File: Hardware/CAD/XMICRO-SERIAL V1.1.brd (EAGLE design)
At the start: 203.2 x 101.6 mm, 92 parts, among them J1 D9-MPH, J2 D9-MPH, J3 MINI-DIN6, J4 PINHD1X3, J5 PINHD1X3, Q1 2N5088, Q2 2N5088, Q3 2N5088, U1 555, U10 74280, U11 74273, U12 74164, U13 74164, U14 7474, U15 74244, U16 74244, U17 74240, U18 74280, U19 74165, U2 7486, U20 74165, U21 74244, U22 7404, U23 74245, U24 16550, U25 16550, U26 75185, U27 75185, U3 7410, U4 7404, U5 7474, U6 7474, U7 7408, U8 74138, U9 74138, Y1 1.8432MHz

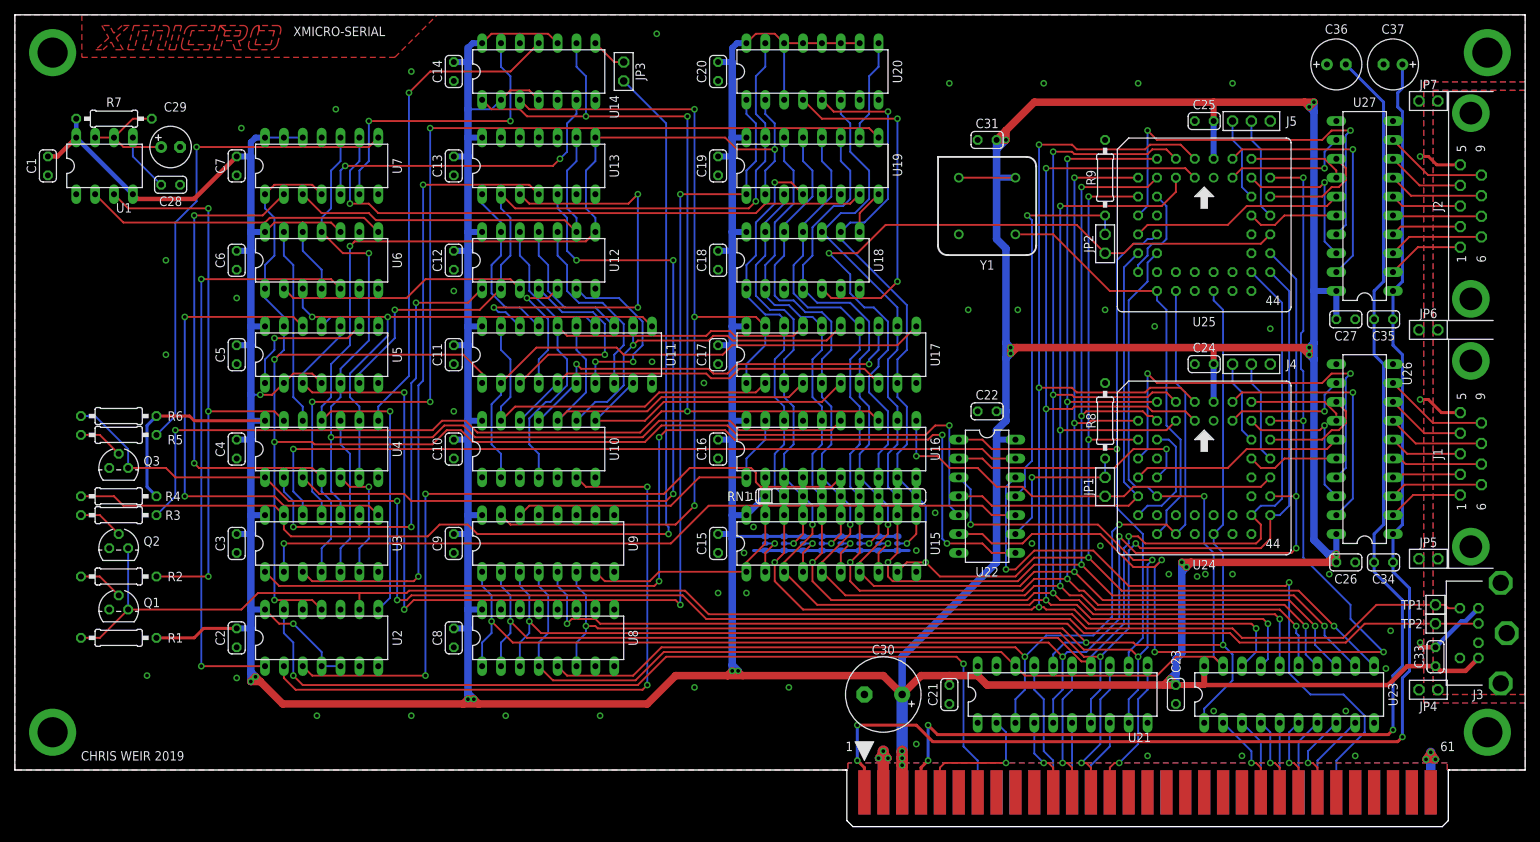
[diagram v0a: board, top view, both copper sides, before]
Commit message: Updated design to V1.1 - added Schmitt trigger inputs, improved connector spacing, fixed PS/2 connector footprint
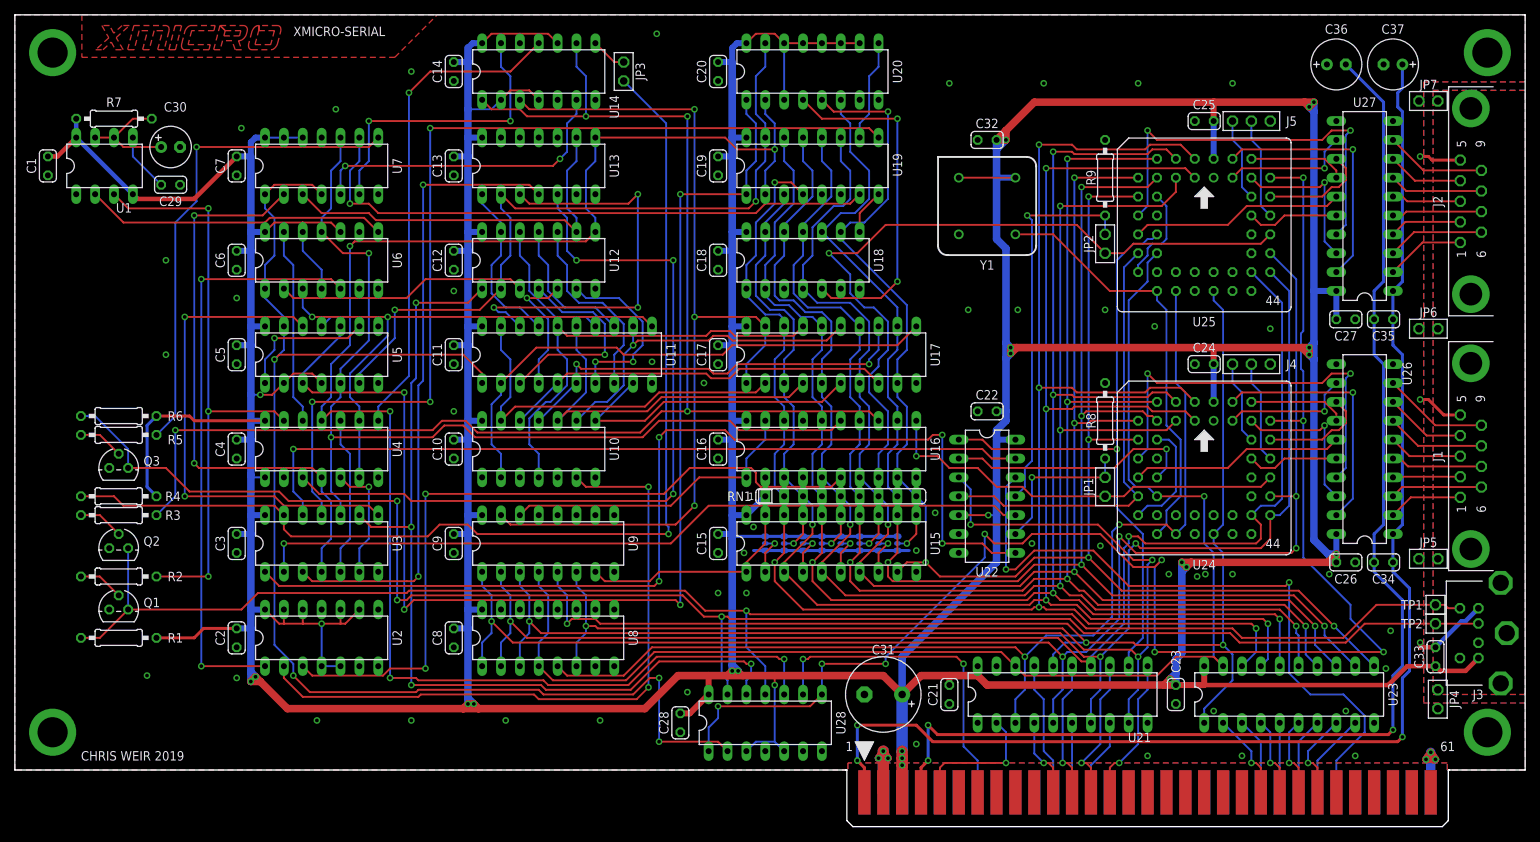
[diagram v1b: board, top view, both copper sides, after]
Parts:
- added C32: 0.1uF, Custom:C100
- added U28: 7414, 74xx-us:DIL14
- C28: value 10nF -> 0.1uF
- C29: value 0.1uF -> 10nF; device rcl:E2,5-6 -> Custom:C100
- C30: value 220uF -> 0.1uF; device Custom:C-10-5 -> rcl:E2,5-6
- C31: value 0.1uF -> 220uF; device Custom:C100 -> Custom:C-10-5
- moved C30 120.9 mm to (21.0, 83.8), turned to 0 degrees
- moved C28 99.7 mm to (89.5, 6.35), turned to 270 degrees
- moved C31 75.9 mm to (116.8, 10.2)
- moved C29 5.08 mm to (21.0, 78.7)
- moved JP4 1.80 mm to (191.5, 9.53), turned to 90 degrees
- moved J2 0.64 mm to (195.9, 76.5)
- moved J1 0.32 mm to (195.9, 42.2)
- moved JP6 0.16 mm to (190.2, 59.4)
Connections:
- removed net N$26: U22.6, U24.39, U25.39
- new net RST: U24.39, U25.39, U28.1, U28.8
- net !BRST: now also U28.9; no longer U2.13
- net !KB_DATA: now also U28.12; no longer U4.2
- net !RST: now also U28.2; no longer U2.11, U22.5
- net BUFF_KB_CLOCK: now also U28.10; no longer U2.8
- net GND: now also C29.P$2, C31.-, C32.P$2, U28.7; no longer C29.-, C31.P$2, U2.10, U2.12
- net KB_CLOCK: now also U28.11; no longer U2.9
- net KB_DATA: now also U28.13; no longer U4.1
- net N$133: now also C30.+; no longer C29.+
- net N$140: now also C29.P$1; no longer C28.P$1
- net VCC: now also C28.P$1, C31.+, C32.P$1, U2.10, U2.12, U2.13, U2.9, U22.5, U28.14, U28.3, U28.5, U4.1; no longer C30.+, C31.P$1
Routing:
- net RST: track 0.00 -> 205.0 mm, vias 0 -> 9
- net N$26: track 151.6 -> 0.00 mm, vias 5 -> 0
- net !BRST: track 120.2 -> 45.0 mm
- net BUFF_KB_CLOCK: track 152.6 -> 221.0 mm, vias 3 -> 5
- net !KB_DATA: track 64.8 -> 121.1 mm, vias 3 -> 4
- net VCC: track 1061.6 -> 1106.1 mm, vias 22 -> 24
- net !RST: track 210.3 -> 177.4 mm
- net KB_DATA: track 211.5 -> 222.3 mm, vias 2 -> 3
- net KB_CLOCK: track 203.3 -> 213.4 mm, vias 0 -> 1
- net N$101: track 88.1 -> 89.9 mm
- net KB_ERR: track 101.1 -> 100.6 mm
- net GND: track 80.5 -> 80.3 mm, vias 62 -> 61
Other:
- board text added: "V1.1 1943"
- board text removed: "V1.1 1912"

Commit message: Fixed a schematic issue - added second inverter to BUFF_KB_CLOCK signal.
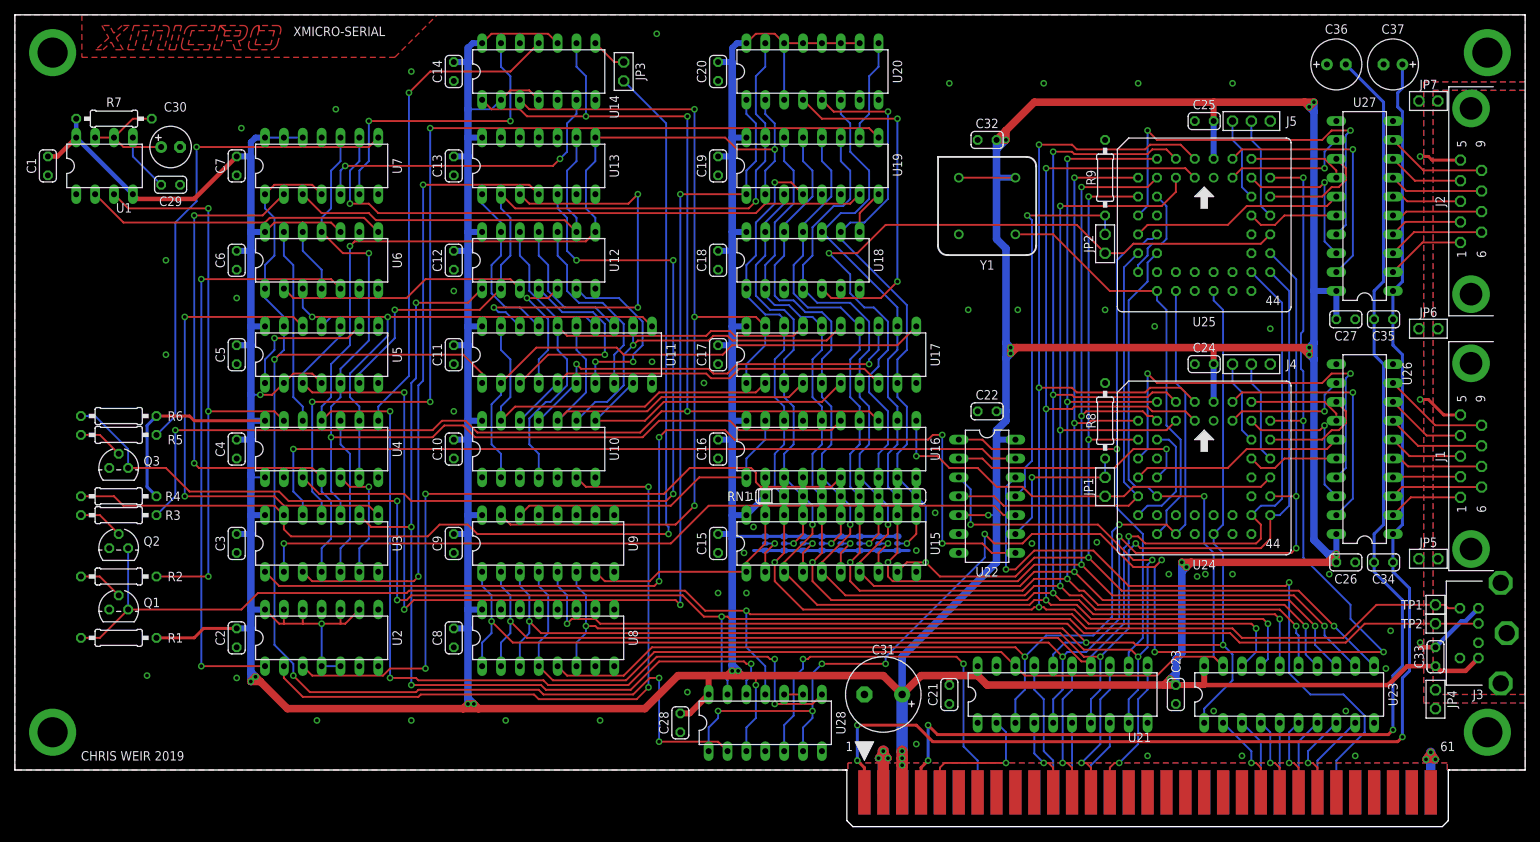
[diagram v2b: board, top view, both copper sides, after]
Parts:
- moved J1 9.53 mm to (205.4, 42.2)
- moved J2 9.53 mm to (205.4, 76.5)
- moved J3 6.35 mm to (205.4, 18.4)
- moved JP4 0.32 mm to (191.1, 9.53)
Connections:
- new net N$26: U28.10, U28.9
- net !BRST: now also U28.5; no longer U28.9
- net BUFF_KB_CLOCK: now also U28.8; no longer U28.10
- net RST: now also U28.6; no longer U28.8
- net VCC: no longer U28.5
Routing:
- net !BRST: track 45.0 -> 53.6 mm
- net BUFF_KB_CLOCK: track 221.0 -> 227.9 mm, vias 5 -> 6
- net RST: track 205.0 -> 211.1 mm, vias 9 -> 10
- net VCC: track 1106.1 -> 1101.8 mm
- net N$26: track 0.00 -> 2.54 mm
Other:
- board text added: "J1 INT"
- board text added: "J2 INT"
- board text added: "KB INT"

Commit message: Updated to hardware V1.1.
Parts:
- removed C35: 0.1uF, Custom:C100
- removed C36, C37: 100uF, rcl:E2,5-7
- added C38, C39: 10uF, rcl:E2,5-5
- added C40: 0.1uF, Custom:C100
- added U29: TC962, Custom:DIL8
- C34: value 0.1uF -> 10uF; device Custom:C100 -> rcl:E2,5-5
- RN1: device resistor-sil:SIL9 -> Custom:SIL9
- moved C34 62.6 mm to (125.4, 49.5), turned to 90 degrees
- moved C32 7.94 mm to (130.8, 92.7)
- moved Y1 7.94 mm to (130.8, 83.8)
- moved C26 2.54 mm to (181.6, 27.9)
- moved C27 2.54 mm to (181.6, 60.6)
- moved JP3 2.54 mm to (84.5, 94.0)
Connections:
- new net N$27: C38.-, U29.4
- new net N$43: C38.+, U29.2
- net +12V: now also C34.+, C40.P$1, U29.8; no longer C34.P$1, C35.P$1, C37.+
- net -12V: now also C39.-, U29.5; no longer C34.P$2, C35.P$2, C36.-, CE0.7
- net GND: now also C34.-, C39.+, C40.P$2, U29.3; no longer C36.+, C37.-
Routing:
- net -12V: track 170.6 -> 96.5 mm, vias 3 -> 1
- net N$116: track 57.5 -> 67.7 mm, vias 0 -> 2
- net N$27: track 0.00 -> 7.83 mm, vias 0 -> 1
- net VCC: track 1101.8 -> 1109.1 mm
- net N$43: track 0.00 -> 5.29 mm
- net A4: track 146.4 -> 149.1 mm
- net N$25: track 137.7 -> 140.2 mm
- net !INT_KB: track 4.86 -> 7.40 mm
- net INT_UART2: track 100.4 -> 98.6 mm
- net N$118: track 52.0 -> 50.7 mm
- net N$24: track 147.1 -> 146.0 mm
- net +12V: track 177.9 -> 178.9 mm, vias 3 -> 5
- net GND: vias 61 -> 62
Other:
- board text added: "JLCJLCJLCJLC"
- board text added: "PORT 1"
- board text added: "PORT 2"
- board text added: "V1.1 1946"
- board text removed: "Edge of case"
- board text removed: "V1.1 1943"
